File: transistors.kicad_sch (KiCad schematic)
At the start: 16 parts, among them J11 Transistor_2, J12 Transistor_1, J13 Transistor_4, J14 Transistor_.3, Q1 DMN2011UTS, Q2 DMN2011UTS, Q3 DMN2011UTS, Q4 DMN2011UTS

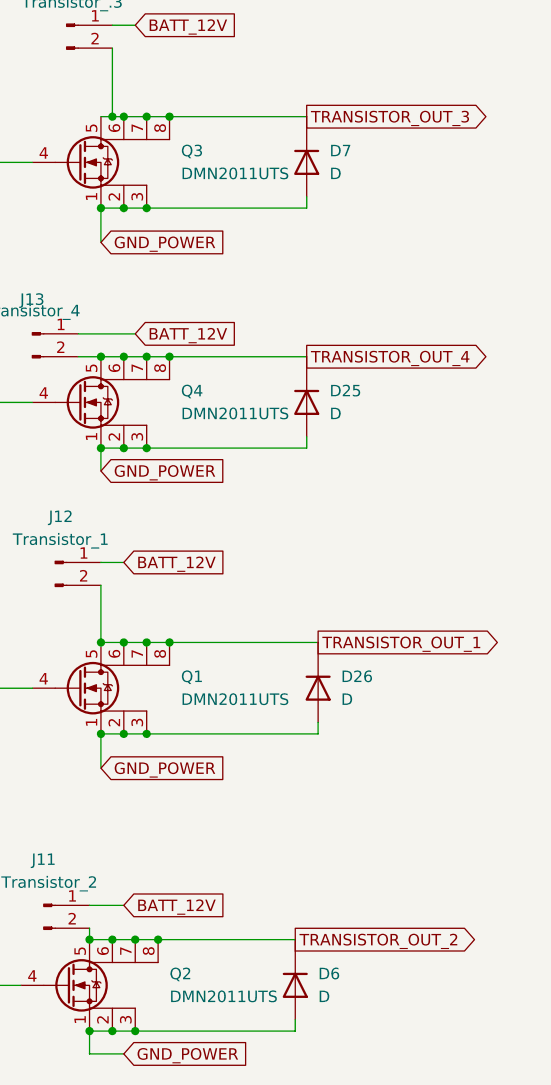
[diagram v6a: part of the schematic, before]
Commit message: Add BOM
Add LCSC reference and correct few footprint acording bom
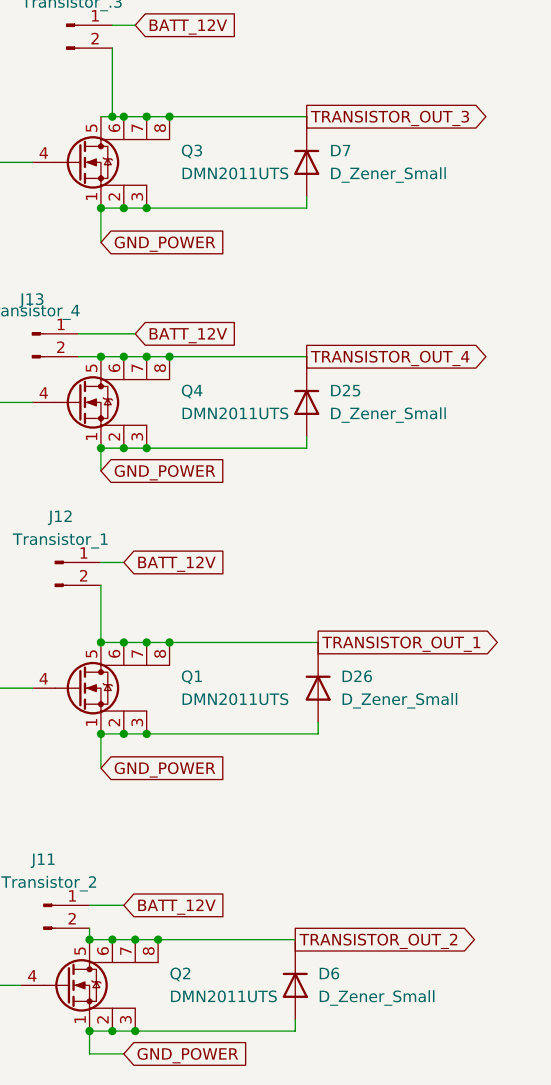
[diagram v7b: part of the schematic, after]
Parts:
- D25, D26, D6, D7: value D -> D_Zener_Small; footprint Diode_SMD:D_1206_3216Metric -> Diode_SMD:D_SOD-123; LCSC# (none) -> C908230
- J11, J12, J13, J14: LCSC# (none) -> C158012
- Q1, Q2, Q3, Q4: LCSC# (none) -> C5245271
- R17, R18, R19, R20: LCSC# (none) -> C2907127
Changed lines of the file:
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@@
+			)
+		)
+		(property "LCSC#" "C158012"
+			(at 181.61 74.93 0)
+			(effects
+				(font
+					(size 1.27 1.27)
+				)
+				(hide yes)
 			)
 		)
@@
 			)
 		)
-		(property "Value" "D"
+		(property "Value" "D_Zener_Small"
 			(at 215.9 115.5699 90)
 			(effects
@@
 			)
 		)
-		(property "Footprint" "Diode_SMD:D_1206_3216Metric"
+		(property "Footprint" "Diode_SMD:D_SOD-123"
 			(at 213.36 114.3 0)
 			(effects
@@
 			)
 		)
-		(property "Sim.Device" "D"
-			(at 213.36 114.3 0)
-			(effects
-				(font
-					(size 1.27 1.27)
-				)
-				(hide yes)
-			)
-		)
-		(property "Sim.Pins" "1=K 2=A"
+		(property "LCSC#" "C908230"
 			(at 213.36 114.3 0)
 			(effects
@@
 			)
 		)
+		(property "LCSC#" "C5245271"
+			(at 185.42 147.32 0)
+			(effects
+				(font
+					(size 1.27 1.27)
+				)
+				(hide yes)
+			)
+		)
 		(pin "1"
 		)
@@
 			)
 		)
-		(property "Value" "D"
+		(property "Value" "D_Zener_Small"
 			(at 213.36 148.5899 90)
 			(effects
@@
 			)
 		)
-		(property "Footprint" "Diode_SMD:D_1206_3216Metric"
+		(property "Footprint" "Diode_SMD:D_SOD-123"
 			(at 210.82 147.32 0)
 			(effects
@@
 			)
 		)
-		(property "Sim.Device" "D"
-			(at 210.82 147.32 0)
-			(effects
-				(font
-					(size 1.27 1.27)
-				)
-				(hide yes)
-			)
-		)
-		(property "Sim.Pins" "1=K 2=A"
+		(property "LCSC#" "C908230"
 			(at 210.82 147.32 0)
 			(effects
@@
 			)
 		)
+		(property "LCSC#" "C2907127"
+			(at 171.45 147.32 0)
+			(effects
+				(font
+					(size 1.27 1.27)
+				)
+				(hide yes)
+			)
+		)
 		(pin "1"
 		)
@@
 			)
 		)
-		(property "Value" "D"
+		(property "Value" "D_Zener_Small"
 			(at 214.63 83.8199 90)
 			(effects
@@
 			)
 		)
-		(property "Footprint" "Diode_SMD:D_1206_3216Metric"
+		(property "Footprint" "Diode_SMD:D_SOD-123"
 			(at 212.09 82.55 0)
 			(effects
@@
 			)
 		)
-		(property "Sim.Device" "D"
-			(at 212.09 82.55 0)
-			(effects
-				(font
-					(size 1.27 1.27)
-				)
-				(hide yes)
-			)
-		)
-		(property "Sim.Pins" "1=K 2=A"
+		(property "LCSC#" "C908230"
 			(at 212.09 82.55 0)
 			(effects
@@
 			)
 		)
+		(property "LCSC#" "C2907127"
+			(at 173.99 82.55 0)
+			(effects
+				(font
+					(size 1.27 1.27)
+				)
+				(hide yes)
+			)
+		)
 		(pin "1"
 		)
@@
 			)
 		)
+		(property "LCSC#" "C158012"
+			(at 182.88 138.43 0)
+			(effects
+				(font
+					(size 1.27 1.27)
+				)
+				(hide yes)
+			)
+		)
 		(pin "1"
 		)
@@
 			)
 		)
+		(property "LCSC#" "C158012"
+			(at 185.42 40.64 0)
+			(effects
+				(font
+					(size 1.27 1.27)
+				)
+				(hide yes)
+			)
+		)
 		(pin "1"
 		)
@@
 			)
 		)
-		(property "Value" "D"
+		(property "Value" "D_Zener_Small"
 			(at 214.63 57.1499 90)
 			(effects
@@
 			)
 		)
-		(property "Footprint" "Diode_SMD:D_1206_3216Metric"
+		(property "Footprint" "Diode_SMD:D_SOD-123"
 			(at 212.09 55.88 0)
 			(effects
@@
 			)
 		)
-		(property "Sim.Device" "D"
-			(at 212.09 55.88 0)
-			(effects
-				(font
-					(size 1.27 1.27)
-				)
-				(hide yes)
-			)
-		)
-		(property "Sim.Pins" "1=K 2=A"
+		(property "LCSC#" "C908230"
 			(at 212.09 55.88 0)
 			(effects
@@
 			)
 		)
+		(property "LCSC#" "C2907127"
+			(at 173.99 55.88 0)
+			(effects
+				(font
+					(size 1.27 1.27)
+				)
+				(hide yes)
+			)
+		)
 		(pin "1"
 		)
@@
 			)
 		)
+		(property "LCSC#" "C5245271"
+			(at 186.69 55.88 0)
+			(effects
+				(font
+					(size 1.27 1.27)
+				)
+				(hide yes)
+			)
+		)
 		(pin "1"
 		)
@@
 			)
 		)
+		(property "LCSC#" "C5245271"
+			(at 186.69 114.3 0)
+			(effects
+				(font
+					(size 1.27 1.27)
+				)
+				(hide yes)
+			)
+		)
 		(pin "1"
 		)
@@
 			)
 		)
+		(property "LCSC#" "C5245271"
+			(at 186.69 82.55 0)
+			(effects
+				(font
+					(size 1.27 1.27)
+				)
+				(hide yes)
+			)
+		)
 		(pin "1"
 		)
@@
 			)
 		)
+		(property "LCSC#" "C158012"
+			(at 184.15 100.33 0)
+			(effects
+				(font
+					(size 1.27 1.27)
+				)
+				(hide yes)
+			)
+		)
 		(pin "1"
 		)
@@
 			(at 172.72 114.3 0)
 			(effects
+				(font
+					(size 1.27 1.27)
+				)
+				(hide yes)
+			)
+		)
+		(property "LCSC#" "C2907127"
+			(at 172.72 114.3 0)
+			(effects
